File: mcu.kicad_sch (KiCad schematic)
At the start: 21 parts, among them J1 Buzzer, J2 GPIO, J3 3v3/GND, Q1 MMBT5551, U1 STM32F103C8Tx, X1 Bluetooth, Y1 8MHz

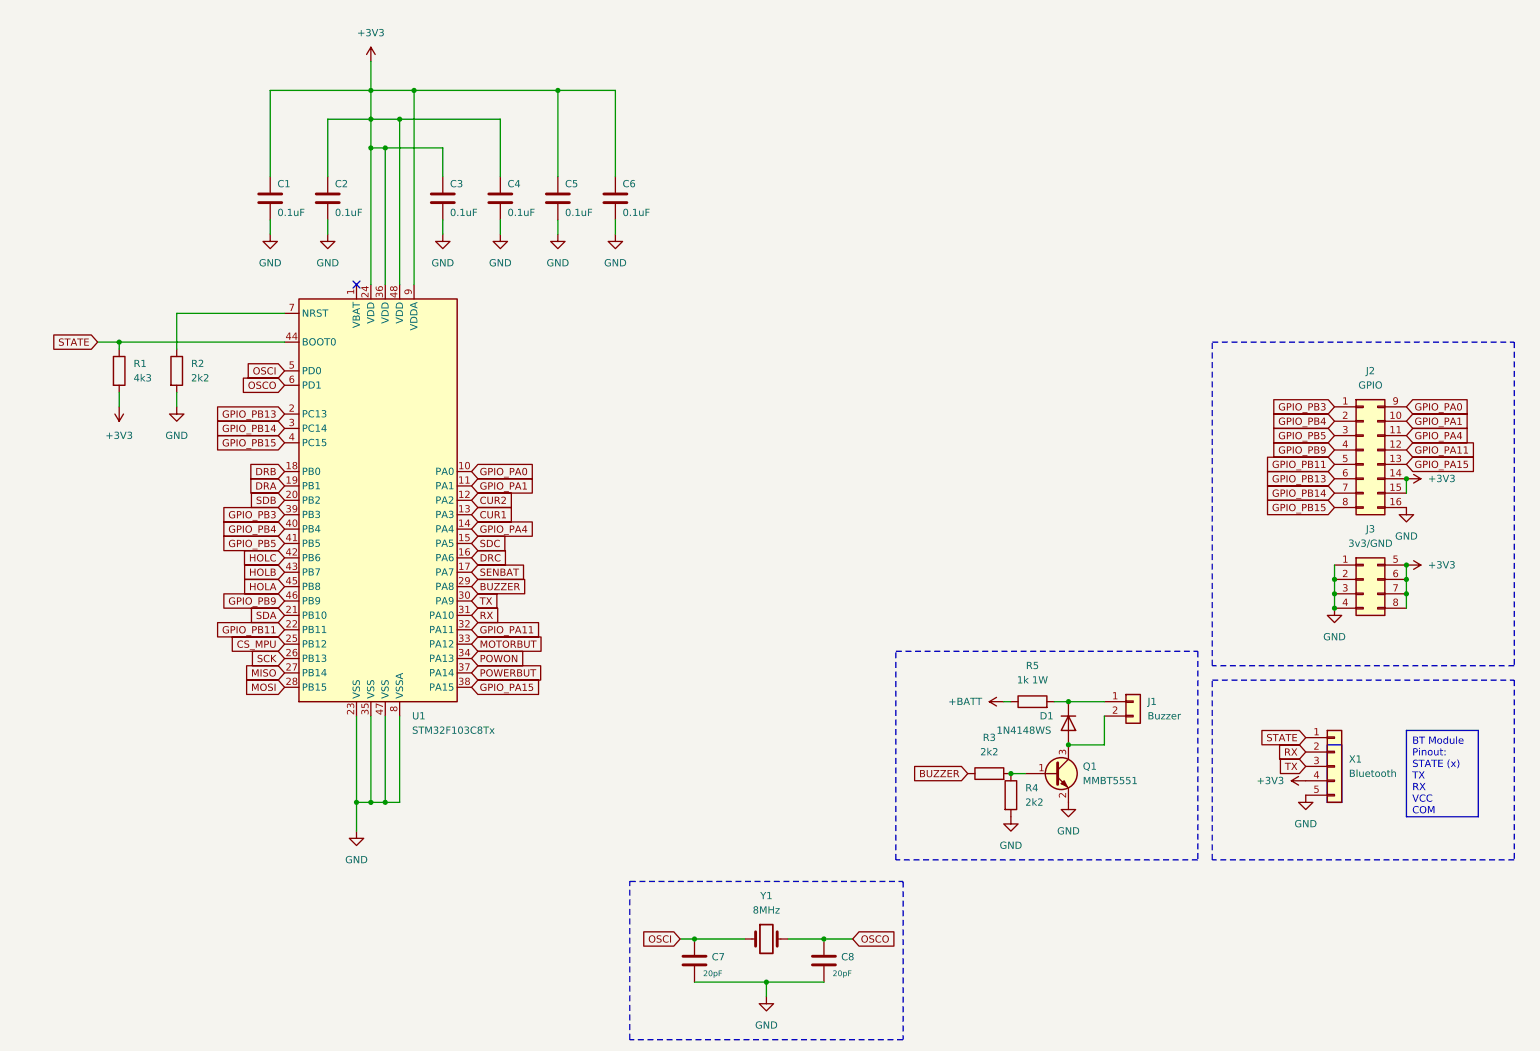
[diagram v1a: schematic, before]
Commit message: Add files via upload
Add +12 and +5 outlets, change buzzer transistor, minor updates
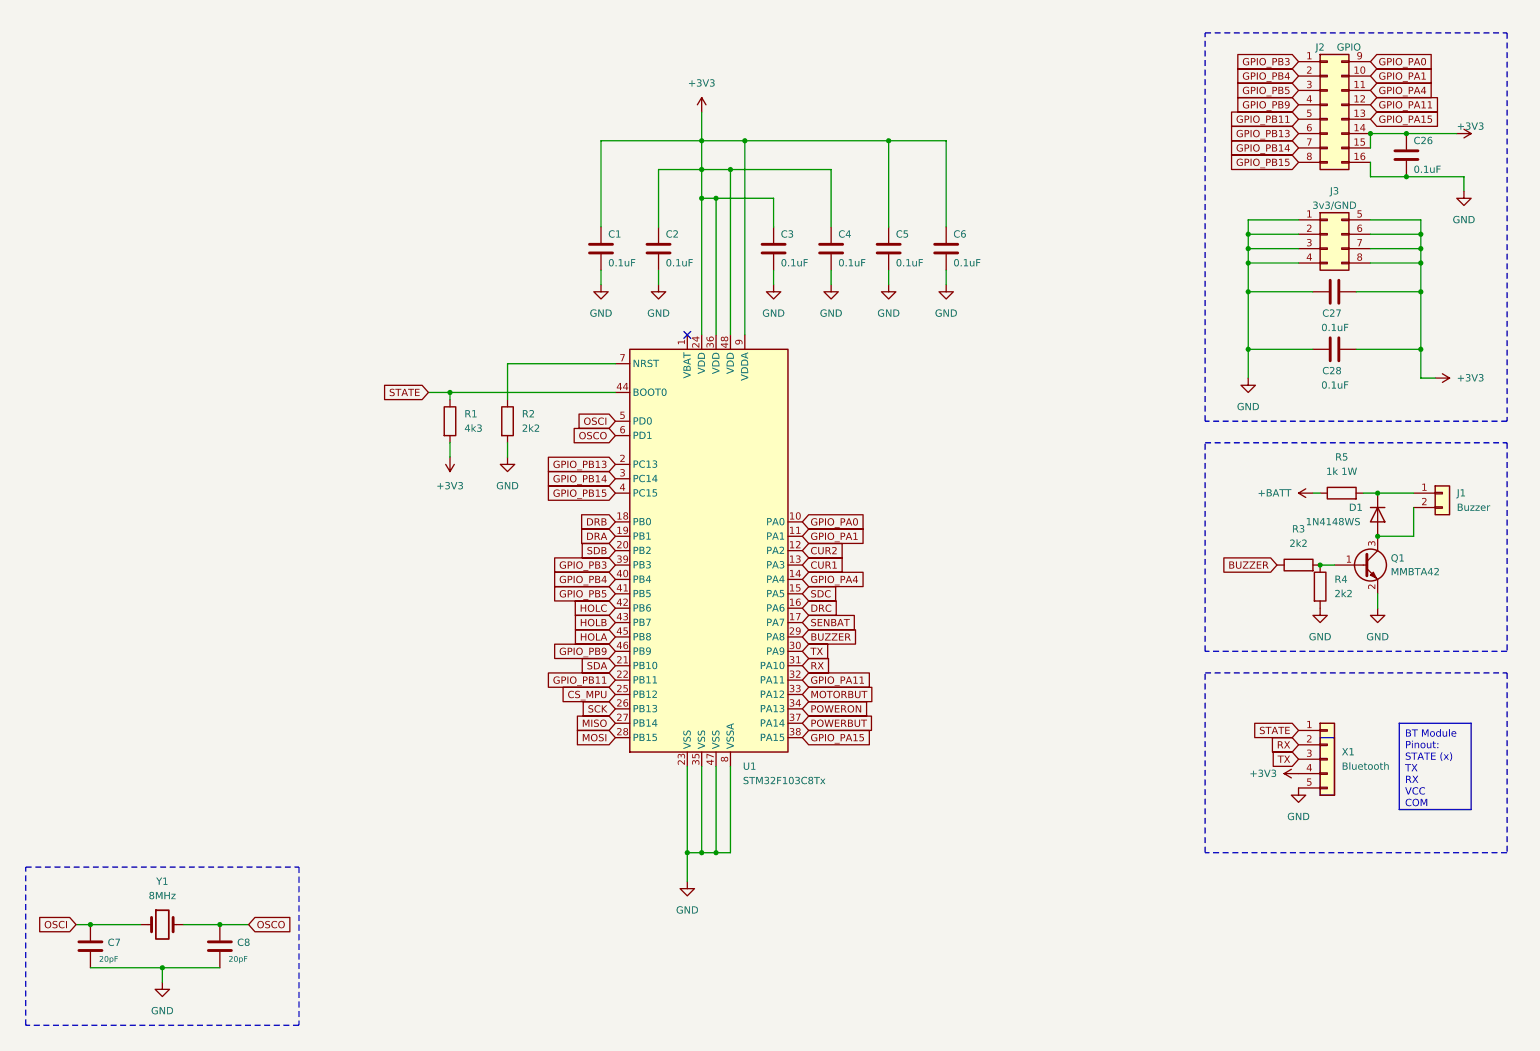
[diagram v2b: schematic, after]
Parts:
- removed Q1: MMBT5551, Package_TO_SOT_SMD_AKL:SOT-23, symbol PCM_Transistor_BJT_AKL:MMBT5551
- added C26, C27, C28: 0.1uF, symbol Device:C
- added Q1: MMBTA42, Package_TO_SOT_SMD:SOT-23, symbol Transistor_BJT:MMBTA42
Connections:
- net +3V3: now also C26.1, C27.2, C28.2
- net GND: now also C26.2, C27.1, C28.1, Q1.2 (E)
- net at D1.2 (A), J1.2 (Pin_2): now also Q1.3 (C)
- net at R3.2, R4.1: now also Q1.1 (B)
- net POWON renamed POWERON
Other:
- moved on the sheet: C1, C2, C3, C4, C5, C6, C7, C8, D1, J1, J2, J3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

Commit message: Divider, gate, mtr button, testpoints, minors
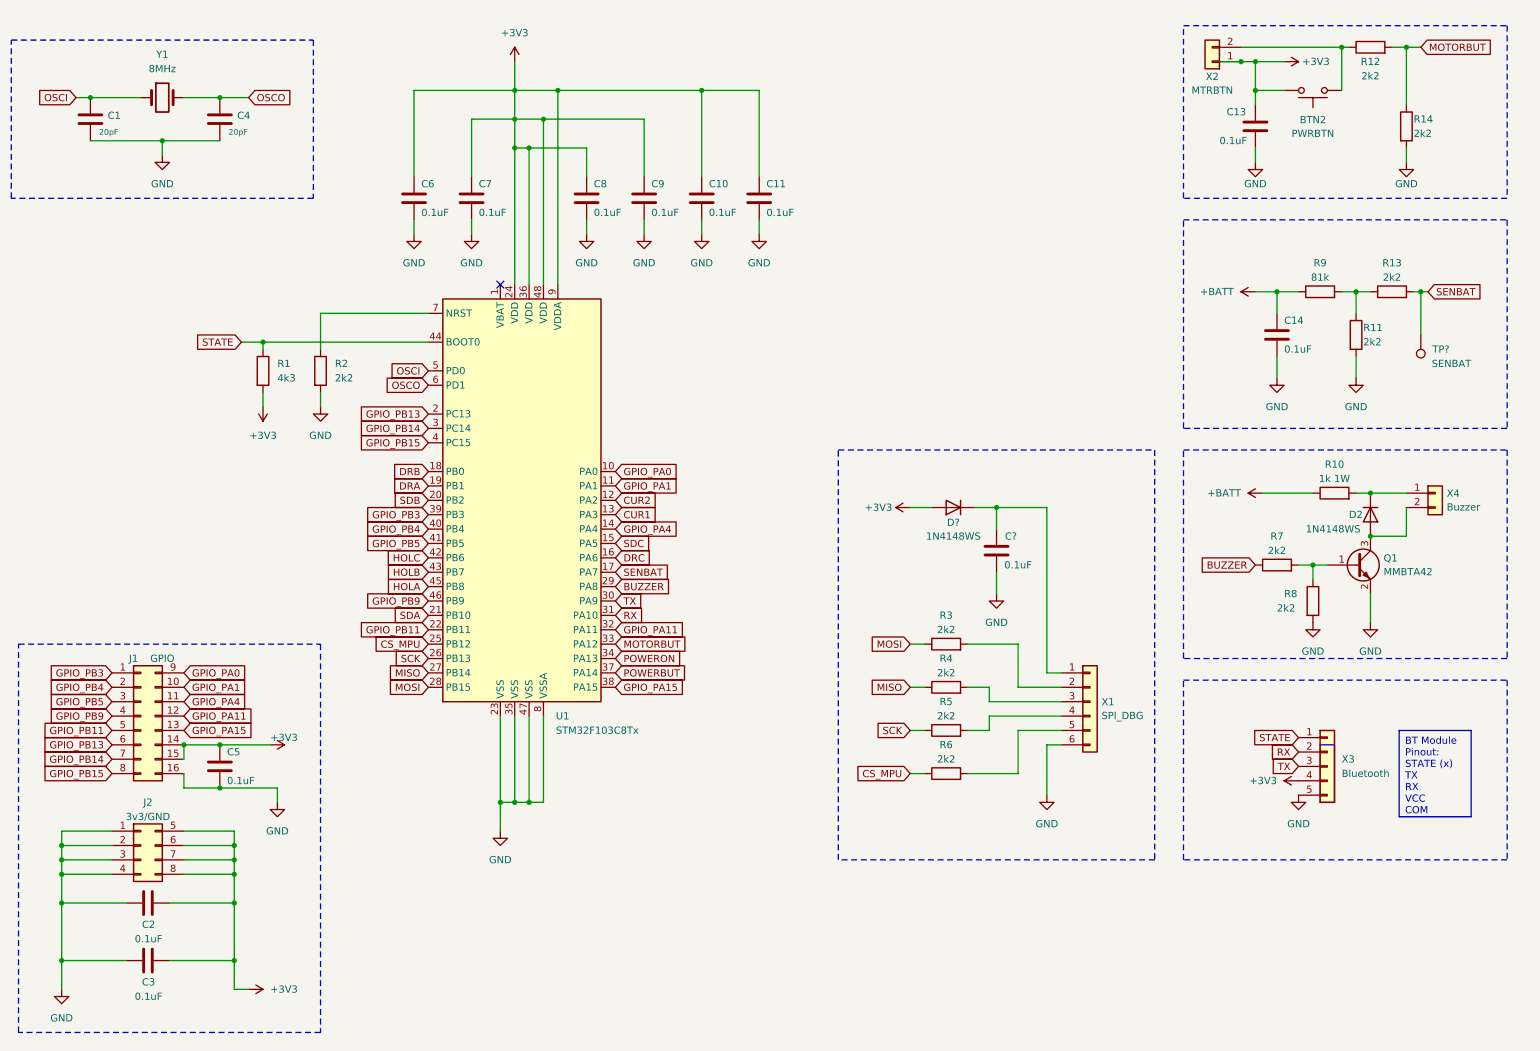
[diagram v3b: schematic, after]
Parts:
- added BTN2: PWRBTN, symbol Switch:SW_Push
- added C13, C14: 0.1uF, symbol Device:C
- added C?: 0.1uF, Capacitor_SMD:C_0402_1005Metric, symbol Device:C
- added D?: 1N4148WS, Diode_SMD:D_SOD-323, symbol Diode:1N4148WS
- added R11, R12, R13, R14, R3, R4, R5, R6: 2k2, symbol Device:R
- added R9: 81k, symbol Device:R
- added TP?: SENBAT, symbol Connector:TestPoint
- added X1: SPI_DBG, symbol Connector_Generic:Conn_01x06
- added X2: MTRBTN, symbol Connector_Generic:Conn_01x02
- renumbered C7 to C1, C5 to C10, C6 to C11, C27 to C2, C28 to C3, C8 to C4, C26 to C5, C1 to C6, C2 to C7, C3 to C8, C4 to C9, D1 to D2, J2 to J1, J3 to J2, R5 to R10, R3 to R7, R4 to R8, X1 to X3, J1 to X4
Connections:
- net +3V3: now also BTN2.2, C13.1, D?.2 (A), X2.1 (Pin_1)
- net +BATT: now also C14.1, R9.1
- net CS_MPU: now also R6.1
- net GND: now also C13.2, C14.2, C?.2, R11.2, R14.2, X1.6 (Pin_6)
- net MISO: now also R4.1
- net MOSI: now also R3.1
- net MOTORBUT: now also R12.2, R14.1
- net SCK: now also R5.1
- net SENBAT: now also R13.2, TP?.1
- new net: R6.2, X1.5 (Pin_5)
- new net: R5.2, X1.4 (Pin_4)
- new net: R4.2, X1.3 (Pin_3)
- new net: C?.1, D?.1 (K), X1.1 (Pin_1)
- new net: BTN2.1, R12.1, X2.2 (Pin_2)
- new net: R11.1, R13.1, R9.2
- new net: R3.2, X1.2 (Pin_2)
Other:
- moved on the sheet: C1, C10, C11, C2, C3, C4, C5, C6, C7, C8, C9, D2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

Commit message: Minors, annotation
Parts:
- gave numbers to parts that had none: 3
- renumbered BTN2 to BTN1
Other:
- note added: "91k for 134v"
- note added: "BLE UART"
- note added: "Buzzer"
- note added: "Clock"
- note added: "External SPI"
- note added: "Motor stop button"
- note added: "Unused GPIO"
- note added: "Voltage Measurement"
- title: (none) -> RedShift-117.6-LogicBoard-F103
- moved on the sheet: BTN1, C12, C13, C14, C2, C3, C5, D1, D2, J1, J2, Q1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

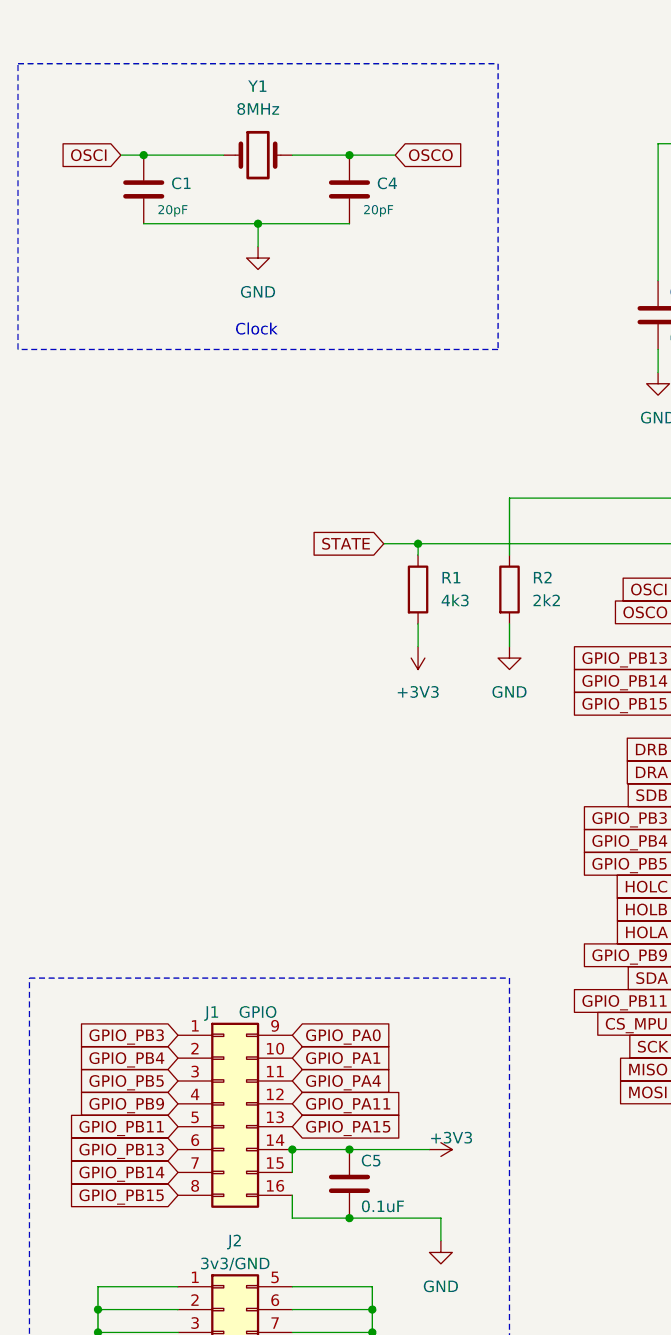
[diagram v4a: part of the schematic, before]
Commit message: Add footprints, fixed xtal
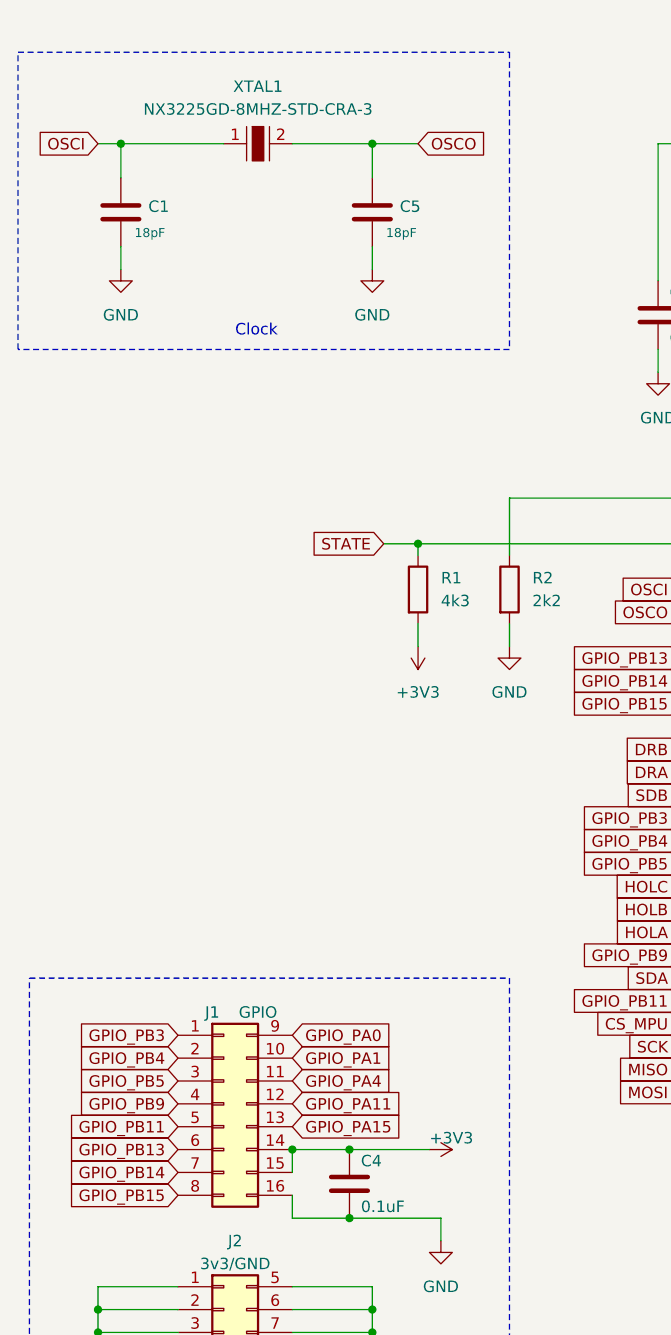
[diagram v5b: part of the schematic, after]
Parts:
- removed C4: 20pF, Capacitor_SMD:C_0201_0603Metric_Pad0.64x0.40mm_HandSolder, symbol Device:C
- removed Y1: 8MHz, ABS07-32:XTAL_ABS07-32.768KHZ-T, symbol Device:Crystal
- added C5: 18pF, Capacitor_SMD:C_0402_1005Metric_Pad0.74x0.62mm_HandSolder, symbol Device:C
- added XTAL1: NX3225GD-8MHZ-STD-CRA-3, digikey-footprints:SMD-2_3.2x2.5mm, symbol dk_Crystals:NX3225GD-8MHZ-STD-CRA-3
- BTN1: footprint (none) -> Button_Switch_SMD:SW_SPST_SKQG_WithoutStem
- C1: value 20pF -> 18pF; footprint Capacitor_SMD:C_0201_0603Metric_Pad0.64x0.40mm_HandSolder -> Capacitor_SMD:C_0402_1005Metric_Pad0.74x0.62mm_HandSolder
- C10, C11, C13, C2, C3, C6, C7, C8, C9: footprint (none) -> Capacitor_SMD:C_0603_1608Metric_Pad1.08x0.95mm_HandSolder
- C12: footprint Capacitor_SMD:C_0402_1005Metric -> Capacitor_SMD:C_0603_1608Metric_Pad1.08x0.95mm_HandSolder
- C14: footprint (none) -> Capacitor_SMD:C_0805_2012Metric_Pad1.18x1.45mm_HandSolder
- C4: renamed from C5; footprint (none) -> Capacitor_SMD:C_0603_1608Metric_Pad1.08x0.95mm_HandSolder
- J1: footprint (none) -> Capacitor_SMD:CP_Elec_10x10.5
- J2: footprint (none) -> Capacitor_SMD:CP_Elec_6.3x7.7
- R1, R11, R12, R13, R14, R2, R3, R4, R5, R6, R7, R8, R9: footprint (none) -> Resistor_SMD:R_0603_1608Metric_Pad0.98x0.95mm_HandSolder
- R10: footprint (none) -> Resistor_SMD:R_2010_5025Metric_Pad1.40x2.65mm_HandSolder
- TP1: footprint (none) -> TestPoint:TestPoint_Pad_D2.0mm
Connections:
- net GND: now also C5.2
- net OSCI: now also XTAL1.1
- net OSCO: now also C5.1, XTAL1.2
